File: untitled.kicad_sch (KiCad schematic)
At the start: 23 parts, among them J2 USB_C_Receptacle_USB2.0_16P, U2 ESP32-S3-WROOM-1, U3 CP2102N-Axx-xQFN28

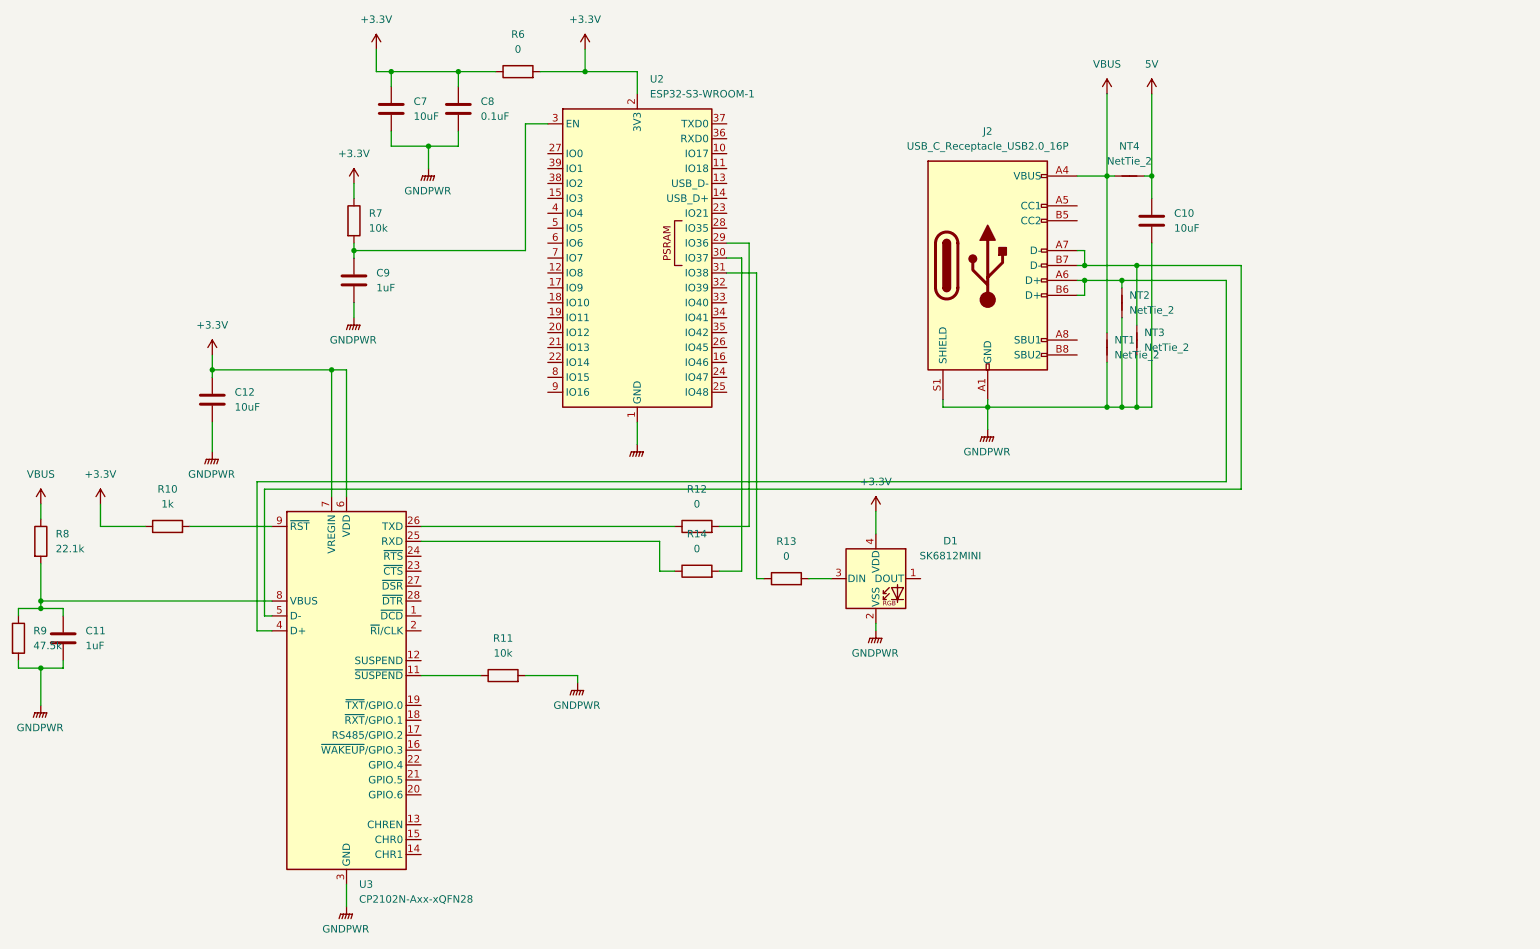
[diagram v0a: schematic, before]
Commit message: added switches and voltage linear regulator
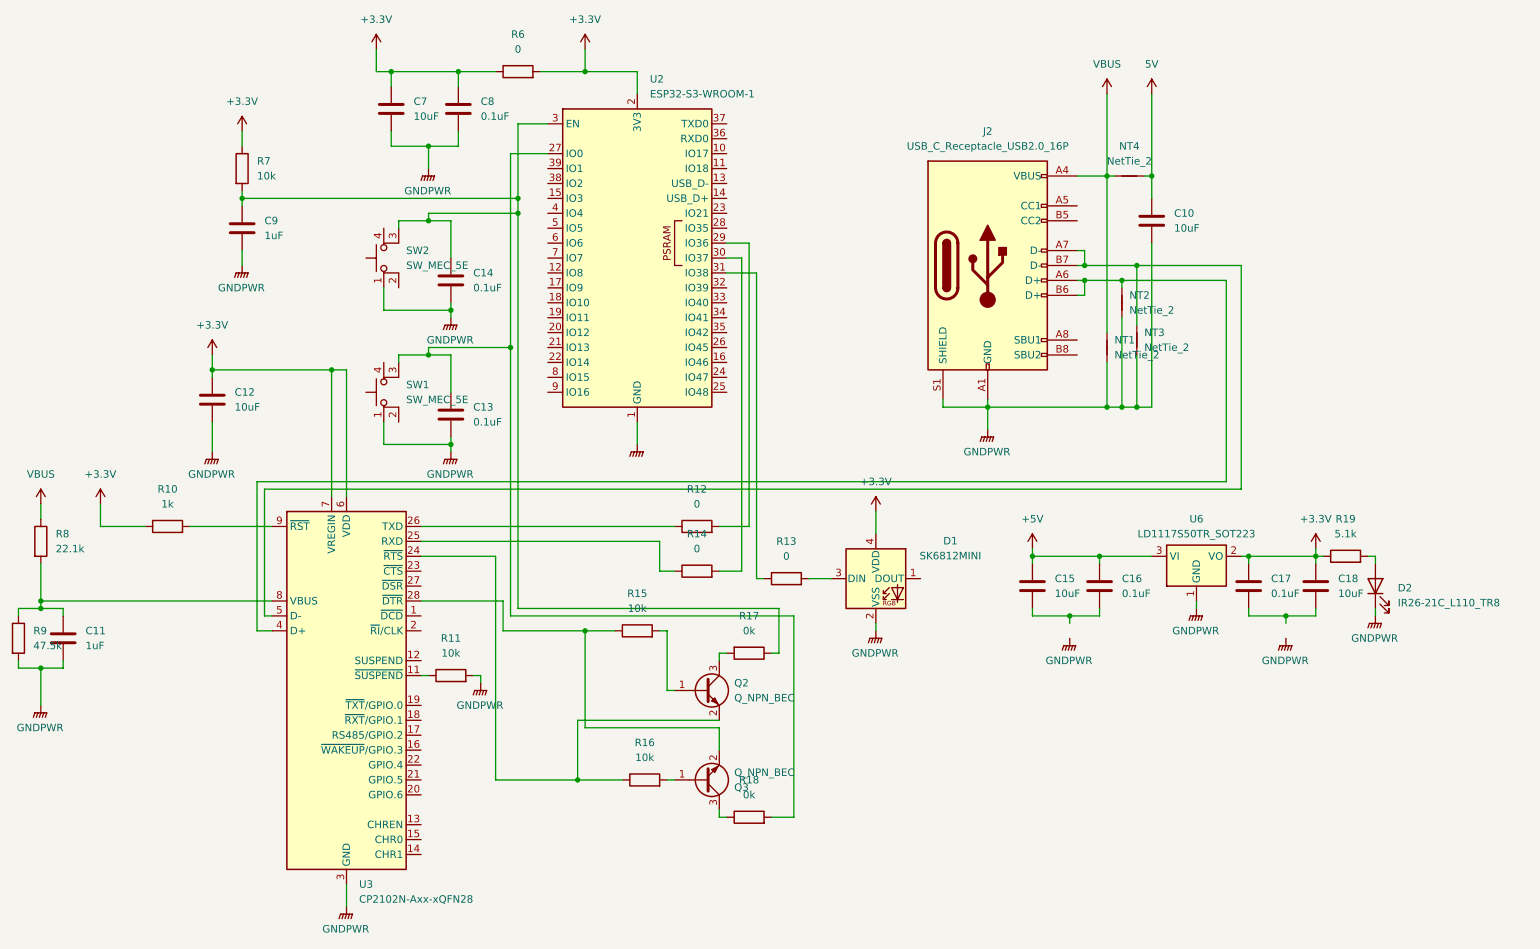
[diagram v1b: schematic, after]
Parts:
- added C13, C14, C16, C17: 0.1uF, symbol Device:C
- added C15, C18: 10uF, symbol Device:C
- added D2: IR26-21C_L110_TR8, LED_SMD:LED_1206_3216Metric, symbol LED:IR26-21C_L110_TR8
- added Q2, Q3: Q_NPN_BEC, symbol Transistor_BJT:Q_NPN_BEC
- added R15, R16: 10k, symbol Device:R
- added R17, R18: 0k, symbol Device:R
- added R19: 5.1k, symbol Device:R
- added SW1, SW2: SW_MEC_5E, symbol Switch:SW_MEC_5E
- added U6: LD1117S50TR_SOT223, Package_TO_SOT_SMD:SOT-223-3_TabPin2, symbol Regulator_Linear:LD1117S50TR_SOT223
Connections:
- net +3.3V: now also C17.1, C18.1, R19.1, U6.2 (VO)
- net GNDPWR: now also C13.2, C14.2, D2.1 (K), SW1.1, SW2.1, U6.1 (GND)
- net at U3.24 (~{RTS}): now also Q2.2 (E), R16.1
- net at U3.28 (~{DTR}): now also Q3.2 (E), R15.1
- net at C9.1, R7.2, U2.3 (EN): now also C14.1, R17.1, SW2.3 (K)
- net at U2.27 (IO0): now also C13.1, R18.2, SW1.3 (K)
- new net: Q2.3 (C), R17.2
- new net: Q3.3 (C), R18.1
- new net: C15.2, C16.2
- new net: D2.2 (A), R19.2
- new net: Q3.1 (B), R16.2
- new net: C17.2, C18.2
- new net: Q2.1 (B), R15.2
- new net +5V: C15.1, C16.1, U6.3 (VI)
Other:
- moved on the sheet: C9, R11, R7

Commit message: changes after 2-26 work meeting
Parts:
- added C19: 10uF, symbol Device:C
- added C20: 0.1uF, symbol Device:C
- added J3, J4: Conn_01x22_Pin, symbol Connector:Conn_01x22_Pin
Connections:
- net 5V is gone; now on net +5V: C10.1, NT4.2
- net +3.3V: now also C19.1, C20.1, J3.1 (Pin_1), J3.2 (Pin_2)
- net +5V: now also J3.21 (Pin_21)
- net GNDPWR: now also SW1.2, SW2.2, C19.2, C20.2, J3.22 (Pin_22), J4.1 (Pin_1), J4.21 (Pin_21), J4.22 (Pin_22)
- net IO0: now reaches C13.1, R18.2, SW1.3 (K), U2.27 (IO0)
- net IO0: now also SW1.4 (A), J4.14 (Pin_14)
- net EN: now reaches C14.1, C9.1, R17.1, R7.2, SW2.3 (K), U2.3 (EN)
- net EN: now also SW2.4 (A), J3.3 (Pin_3)
- net D+: now reaches J2.A6 (D+), J2.B6 (D+), NT2.2, U3.4 (D+)
- net D-: now reaches J2.A7 (D-), J2.B7 (D-), NT3.2, U3.5 (D-)
- net GPIO37: now reaches R14.2, U2.30 (IO37)
- net GPIO37: now also J4.11 (Pin_11)
- net GPIO17: now reaches U2.10 (IO17)
- net GPIO17: now also J3.10 (Pin_10)
- net GPIO18: now reaches U2.11 (IO18)
- net GPIO18: now also J3.11 (Pin_11)
- net GPIO8: now reaches U2.12 (IO8)
- net GPIO8: now also J3.12 (Pin_12)
- net GPIO19: now reaches U2.13 (USB_D-)
- net GPIO19: now also J4.20 (Pin_20)
- net GPIO20: now reaches U2.14 (USB_D+)
- net GPIO20: now also J4.19 (Pin_19)
- net GPIO3: now reaches U2.15 (IO3)
- net GPIO3: now also J3.13 (Pin_13)
- net GPIO46: now reaches U2.16 (IO46)
- net GPIO46: now also J3.14 (Pin_14)
- net GPIO9: now reaches U2.17 (IO9)
- net GPIO9: now also J3.15 (Pin_15)
- net GPIO10: now reaches U2.18 (IO10)
- net GPIO10: now also J3.16 (Pin_16)
- net GPIO11: now reaches U2.19 (IO11)
- net GPIO11: now also J3.17 (Pin_17)
- net GPIO12: now reaches U2.20 (IO12)
- net GPIO12: now also J3.18 (Pin_18)
- net GPIO13: now reaches U2.21 (IO13)
- net GPIO13: now also J3.19 (Pin_19)
- net GPIO14: now reaches U2.22 (IO14)
- net GPIO14: now also J3.20 (Pin_20)
- net GPIO21: now reaches U2.23 (IO21)
- net GPIO21: now also J4.18 (Pin_18)
- net GPIO47: now reaches U2.24 (IO47)
- net GPIO47: now also J4.17 (Pin_17)
- net GPIO48: now reaches U2.25 (IO48)
- net GPIO48: now also J4.16 (Pin_16)
- net GPIO45: now reaches U2.26 (IO45)
- net GPIO45: now also J4.15 (Pin_15)
- net GPIO35: now reaches U2.28 (IO35)
- net GPIO35: now also J4.13 (Pin_13)
- net GPIO36: now reaches R12.2, U2.29 (IO36)
- net GPIO36: now also J4.12 (Pin_12)
- net GPIO38: now reaches R13.1, U2.31 (IO38)
- net GPIO38: now also J4.10 (Pin_10)
- net GPIO39: now reaches U2.32 (IO39)
- net GPIO39: now also J4.9 (Pin_9)
- net GPIO40: now reaches U2.33 (IO40)
- net GPIO40: now also J4.8 (Pin_8)
- net GPIO41: now reaches U2.34 (IO41)
- net GPIO41: now also J4.7 (Pin_7)
- net GPIO42: now reaches U2.35 (IO42)
- net GPIO42: now also J4.6 (Pin_6)
- net RXD0: now reaches U2.36 (RXD0)
- net RXD0: now also J4.3 (Pin_3)
- net TXD0: now reaches U2.37 (TXD0)
- net TXD0: now also J4.2 (Pin_2)
- net GPIO2: now reaches U2.38 (IO2)
- net GPIO2: now also J4.5 (Pin_5)
- net GPIO1: now reaches U2.39 (IO1)
- net GPIO1: now also J4.4 (Pin_4)
- net GPIO4: now reaches U2.4 (IO4)
- net GPIO4: now also J3.4 (Pin_4)
- net GPIO5: now reaches U2.5 (IO5)
- net GPIO5: now also J3.5 (Pin_5)
- net GPIO6: now reaches U2.6 (IO6)
- net GPIO6: now also J3.6 (Pin_6)
- net GPIO7: now reaches U2.7 (IO7)
- net GPIO7: now also J3.7 (Pin_7)
- net GPIO15: now reaches U2.8 (IO15)
- net GPIO15: now also J3.8 (Pin_8)
- net GPIO16: now reaches U2.9 (IO16)
- net GPIO16: now also J3.9 (Pin_9)
- no-connect marks 0 -> 15
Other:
- moved on the sheet: C10, C15, C16, C17, C18, D1, D2, J2, NT1, NT2, NT3, NT4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

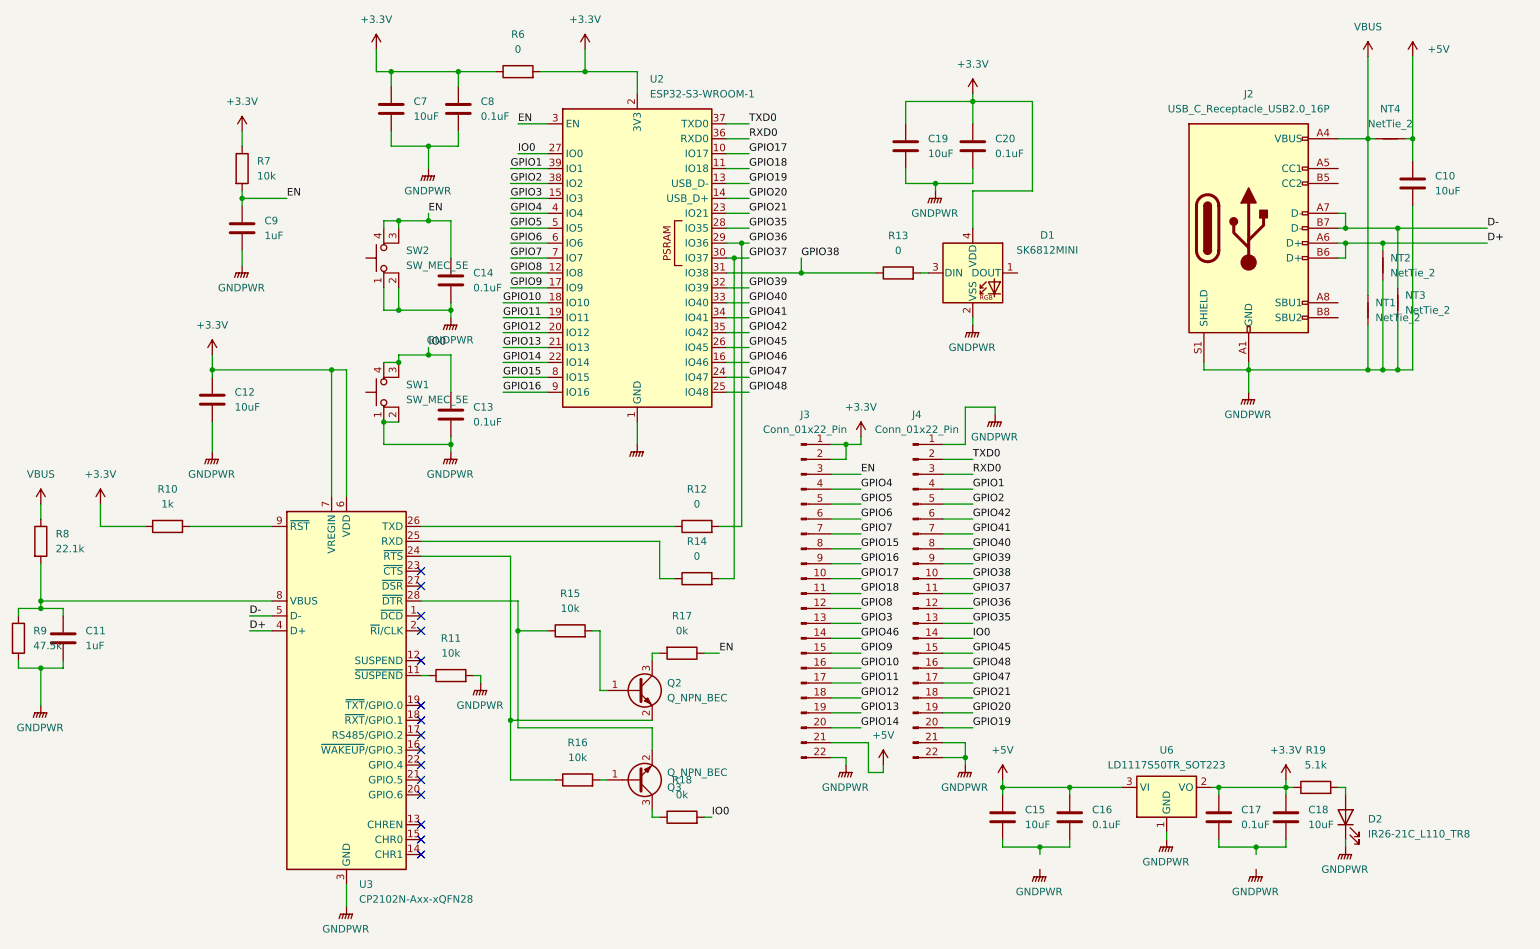
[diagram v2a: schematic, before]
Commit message: updated bjts and connectd cc1 and cc2 on sheettwo
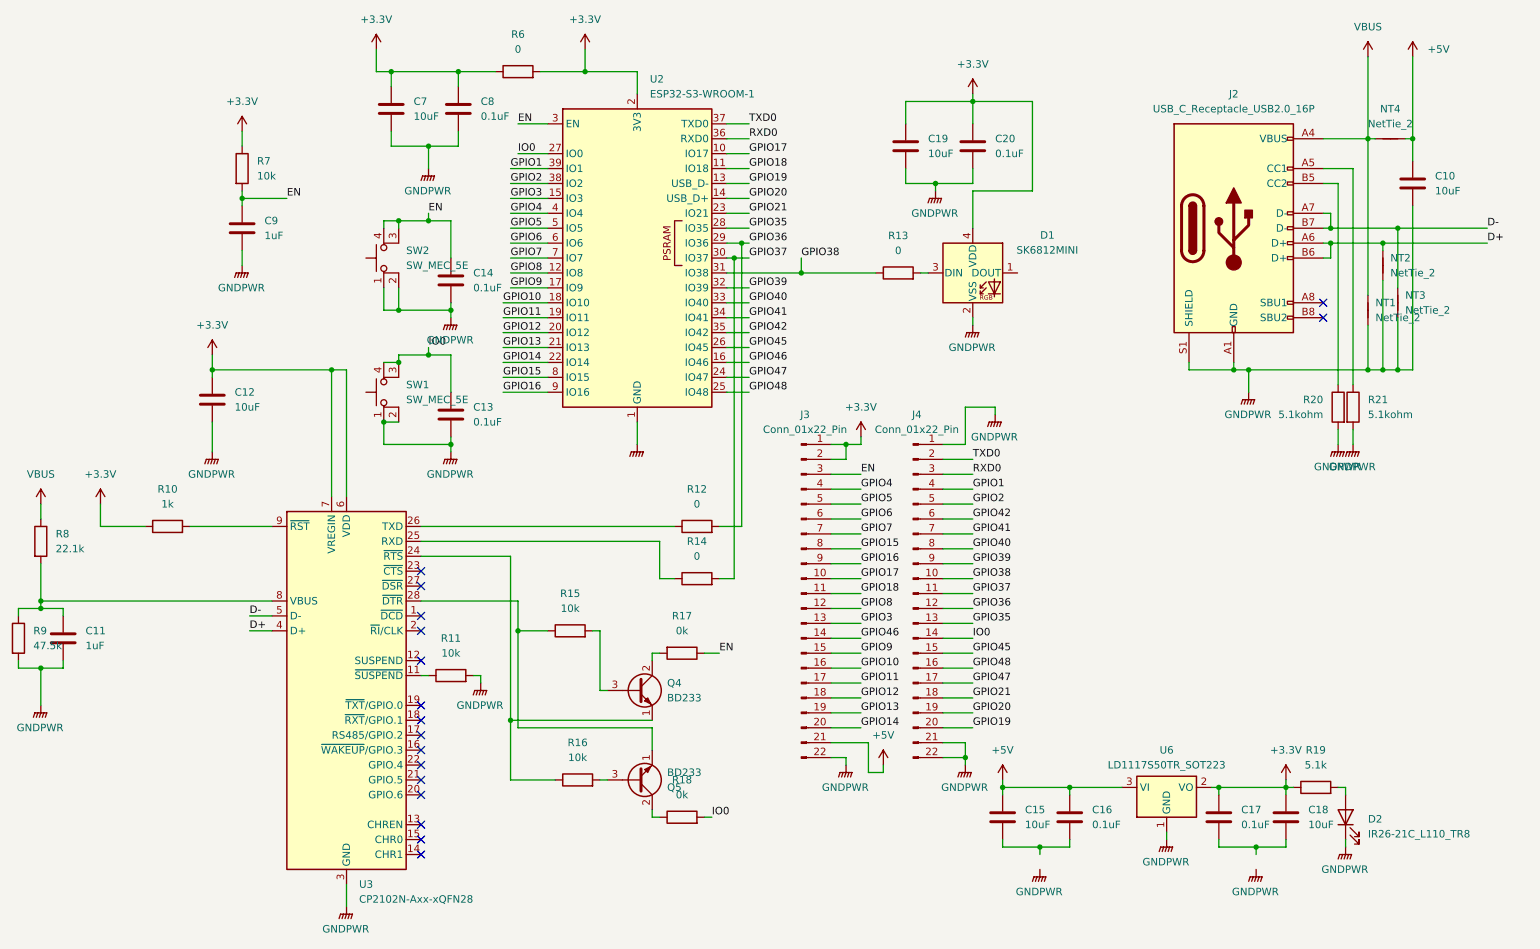
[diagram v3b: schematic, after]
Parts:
- removed Q2, Q3: Q_NPN_BEC, symbol Transistor_BJT:Q_NPN_BEC
- added Q4, Q5: BD233, Package_TO_SOT_THT:TO-126-3_Vertical, symbol Transistor_BJT:BD233
- added R20, R21: 5.1kohm, symbol Device:R
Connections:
- net GNDPWR: now also R20.2, R21.2
- net at R17.2: now also Q4.2 (C)
- net at J2.A5 (CC1): now also R21.1
- net at J2.B5 (CC2): now also R20.1
- net at R16.1, U3.24 (~{RTS}): now also Q4.1 (E)
- net at R15.1, U3.28 (~{DTR}): now also Q5.1 (E)
- net at R18.1: now also Q5.2 (C)
- net at R16.2: now also Q5.3 (B)
- net at R15.2: now also Q4.3 (B)
- no-connect marks 15 -> 17
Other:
- moved on the sheet: J2

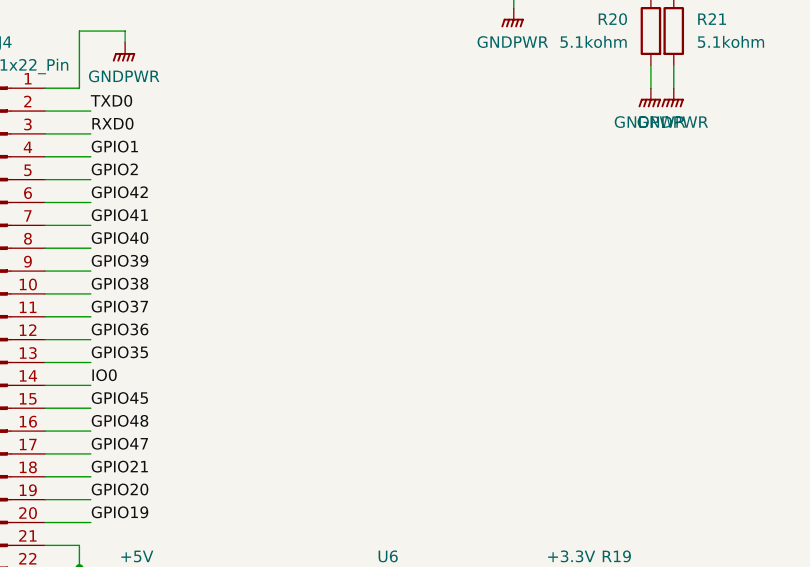
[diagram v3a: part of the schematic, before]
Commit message: need to add buck converter for dc to pd controller
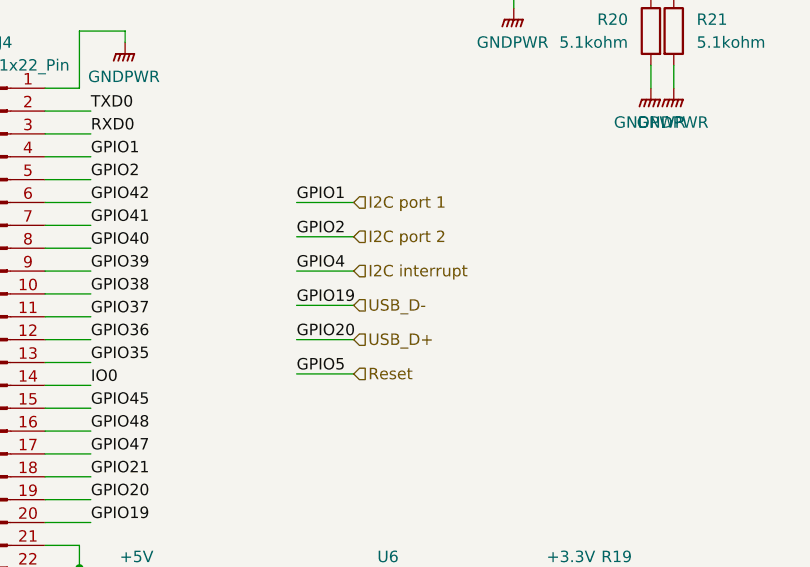
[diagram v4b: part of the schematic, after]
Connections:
- net GPIO1 renamed I2C port 1
- net GPIO19 renamed USB_D-
- net GPIO2 renamed I2C port 2
- net GPIO20 renamed USB_D+
- net GPIO4 renamed I2C interrupt
- net GPIO5 renamed Reset
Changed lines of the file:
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@@
+	(wire
+		(pts
+			(xy 215.9 118.11) (xy 222.25 118.11)
+		)
+		(stroke
+			(width 0)
+			(type default)
+		)
+	)
 	(wire
 		(pts
@@
 	(wire
 		(pts
+			(xy 215.9 99.06) (xy 222.25 99.06)
+		)
+		(stroke
+			(width 0)
+			(type default)
+		)
+	)
+	(wire
+		(pts
 			(xy 114.3 143.51) (xy 121.92 143.51)
 		)
@@
 	(wire
 		(pts
+			(xy 215.9 106.68) (xy 222.25 106.68)
+		)
+		(stroke
+			(width 0)
+			(type default)
+		)
+	)
+	(wire
+		(pts
 			(xy 69.85 118.11) (xy 73.66 118.11)
 		)
@@
 	(wire
 		(pts
+			(xy 215.9 114.3) (xy 222.25 114.3)
+		)
+		(stroke
+			(width 0)
+			(type default)
+		)
+	)
+	(wire
+		(pts
 			(xy 113.03 77.47) (xy 120.65 77.47)
 		)
@@
 	(wire
 		(pts
+			(xy 215.9 102.87) (xy 222.25 102.87)
+		)
+		(stroke
+			(width 0)
+			(type default)
+		)
+	)
+	(wire
+		(pts
 			(xy 114.3 52.07) (xy 120.65 52.07)
 		)
@@
 		(pts
 			(xy 151.13 31.75) (xy 154.94 31.75)
+		)
+		(stroke
+			(width 0)
+			(type default)
+		)
+	)
+	(wire
+		(pts
+			(xy 215.9 110.49) (xy 222.25 110.49)
 		)
 		(stroke
@@
 		)
 	)
+	(label "GPIO20"
+		(at 215.9 114.3 0)
+		(effects
+			(font
+				(size 1.27 1.27)
+			)
+			(justify left bottom)
+		)
+	)
 	(label "GPIO21"
 		(at 154.94 46.99 0)
@@
 		)
 	)
+	(label "GPIO2"
+		(at 215.9 102.87 0)
+		(effects
+			(font
+				(size 1.27 1.27)
+			)
+			(justify left bottom)
+		)
+	)
+	(label "GPIO5"
+		(at 215.9 118.11 0)
+		(effects
+			(font
+				(size 1.27 1.27)
+			)
+			(justify left bottom)
+		)
+	)
 	(label "GPIO14"
 		(at 113.03 72.39 0)
@@
 		)
 	)
+	(label "GPIO4"
+		(at 215.9 106.68 0)
+		(effects
+			(font
+				(size 1.27 1.27)
+			)
+			(justify left bottom)
+		)
+	)
 	(label "GPIO46"
 		(at 154.94 72.39 0)
@@
 		)
 	)
+	(label "GPIO1"
+		(at 215.9 99.06 0)
+		(effects
+			(font
+				(size 1.27 1.27)
+			)
+			(justify left bottom)
+		)
+	)
 	(label "GPIO13"
 		(at 113.03 69.85 0)
@@
 		)
 	)
+	(label "GPIO19"
+		(at 215.9 110.49 0)
+		(effects
+			(font
+				(size 1.27 1.27)
+			)
+			(justify left bottom)
+		)
+	)
 	(label "GPIO1"
 		(at 193.04 93.98 0)
@@
 		)
 	)
+	(hierarchical_label "Reset"
+		(shape input)
+		(at 222.25 118.11 0)
+		(effects
+			(font
+				(size 1.27 1.27)
+			)
+			(justify left)
+		)
+	)
+	(hierarchical_label "I2C port 1"
+		(shape input)
+		(at 222.25 99.06 0)
+		(effects
+			(font
+				(size 1.27 1.27)
+			)
+			(justify left)
+		)
+	)
+	(hierarchical_label "USB_D-"
+		(shape input)
+		(at 222.25 110.49 0)
+		(effects
+			(font
+				(size 1.27 1.27)
+			)
+			(justify left)
+		)
+	)
+	(hierarchical_label "USB_D+"
+		(shape input)
+		(at 222.25 114.3 0)
+		(effects
+			(font
+				(size 1.27 1.27)
+			)
+			(justify left)
+		)
+	)
+	(hierarchical_label "I2C interrupt"
+		(shape input)
+		(at 222.25 106.68 0)
+		(effects
+			(font
+				(size 1.27 1.27)
+			)
+			(justify left)
+		)
+	)
+	(hierarchical_label "I2C port 2"
+		(shape input)
+		(at 222.25 102.87 0)
+		(effects
+			(font
+				(size 1.27 1.27)
+			)
+			(justify left)
+		)
+	)
